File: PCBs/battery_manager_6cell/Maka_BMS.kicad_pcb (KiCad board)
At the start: 2 copper layers, 48.7 x 48.5 mm, 107 parts, among them J2 Conn_02x05_Odd_Even, J7 Conn_01x03, Q1 FDC645N, Q2 FDC645N, Q3 FDC645N, Q4 Si3483CDV, Q5 Si3483CDV, Q6 FDC645N, Q7 FDC645N, Q8 FDC645N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

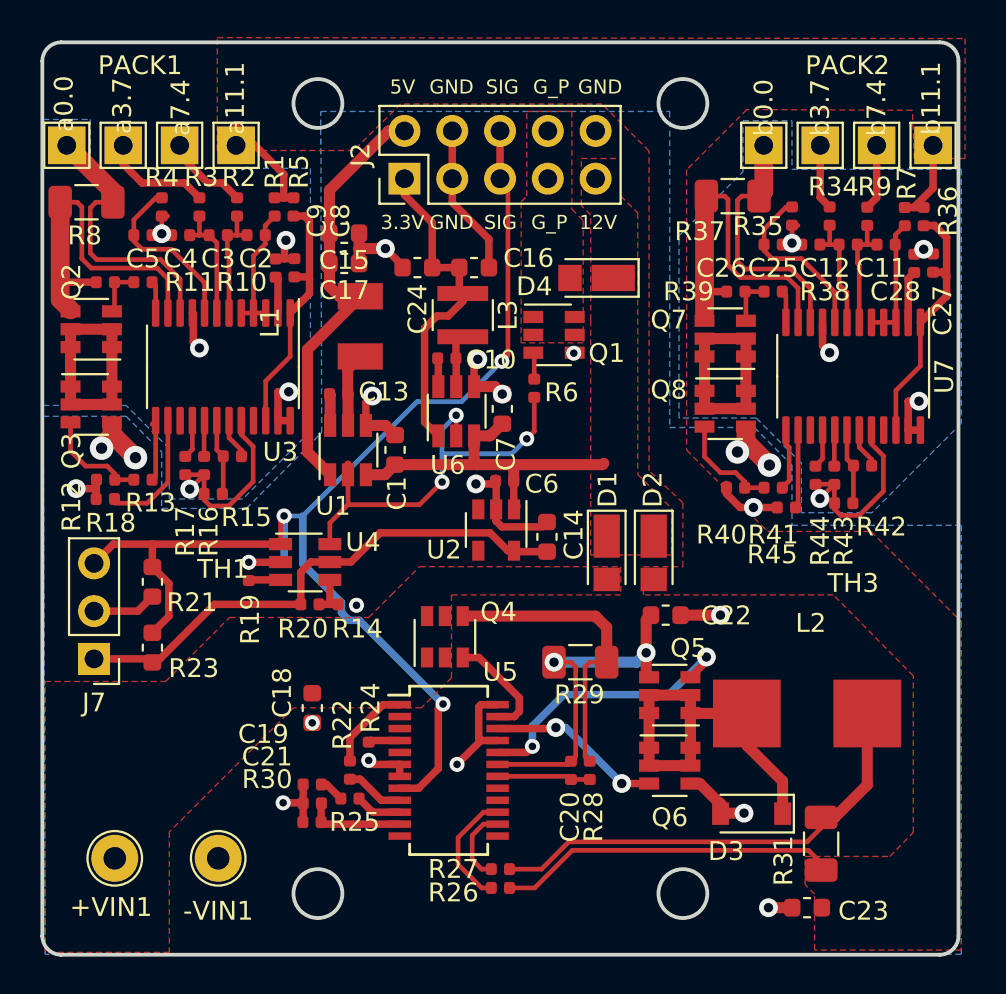
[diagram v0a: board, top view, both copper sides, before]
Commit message: updates to battery managemennt wayfinder boards, and makaniu hall sensor ring and BMS
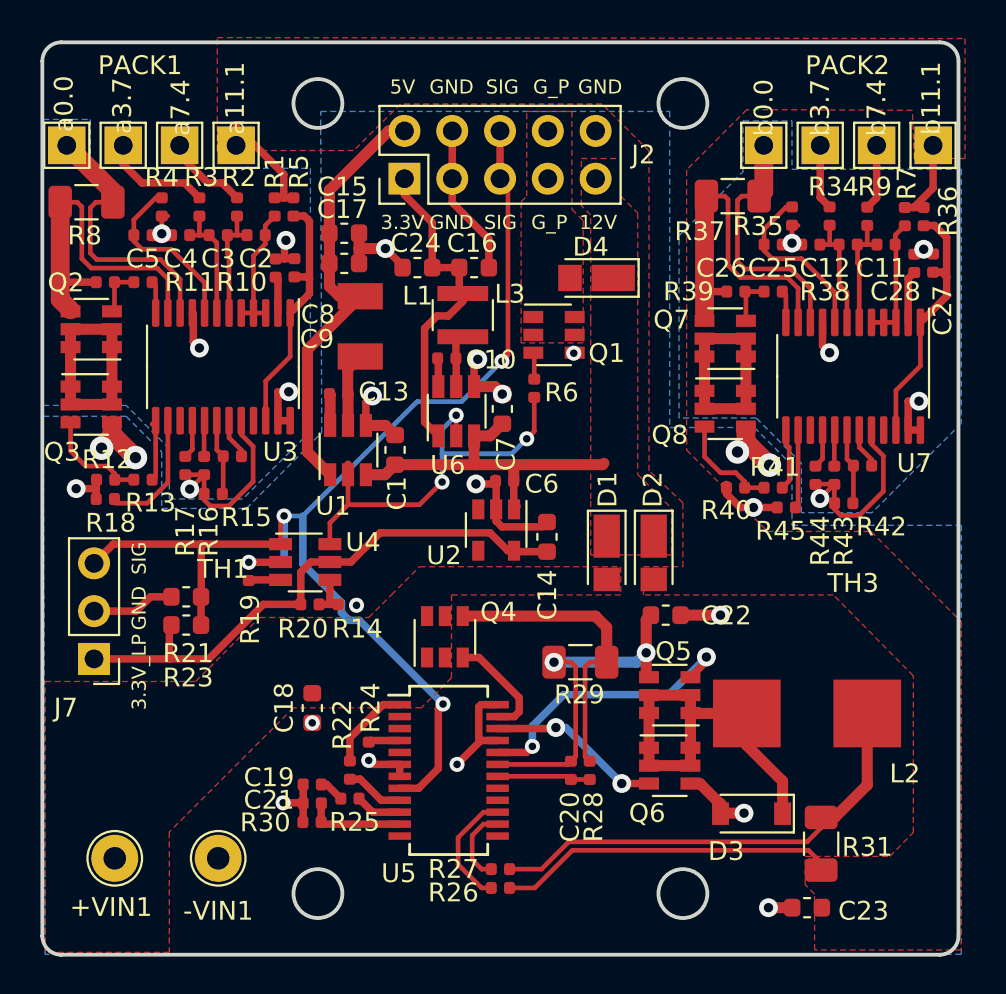
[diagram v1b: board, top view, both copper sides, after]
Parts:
- U2: value TPS70933DBV -> TPS70933QDBVR
- moved R23 2.16 mm to (130.1, 106.0), turned to 0 degrees
- moved R21 1.97 mm to (130.1, 104.5), turned to 180 degrees
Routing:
- net +3V3_LowPwr: track 28.3 -> 30.2 mm
- net ~SHT_DWN_SIG~: track 67.0 -> 65.8 mm
- net Earth: track 59.8 -> 60.9 mm
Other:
- rule trace_min: 0 -> 0.25
- board text added: "3.3V_LP"
